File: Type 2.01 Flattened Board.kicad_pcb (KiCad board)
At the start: 4 copper layers, 170 x 170 mm, 70 parts, among them J1 Conn_02x28_Odd_Even, J2 Conn_01x02, J3 Conn_01x04, J4 Conn_02x03_Odd_Even, J5 Conn_02x03_Odd_Even, J6 Conn_02x28_Odd_Even, U1 74AHC74, U10 74AHC174, U11 74AHC245, U13 74AHC04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

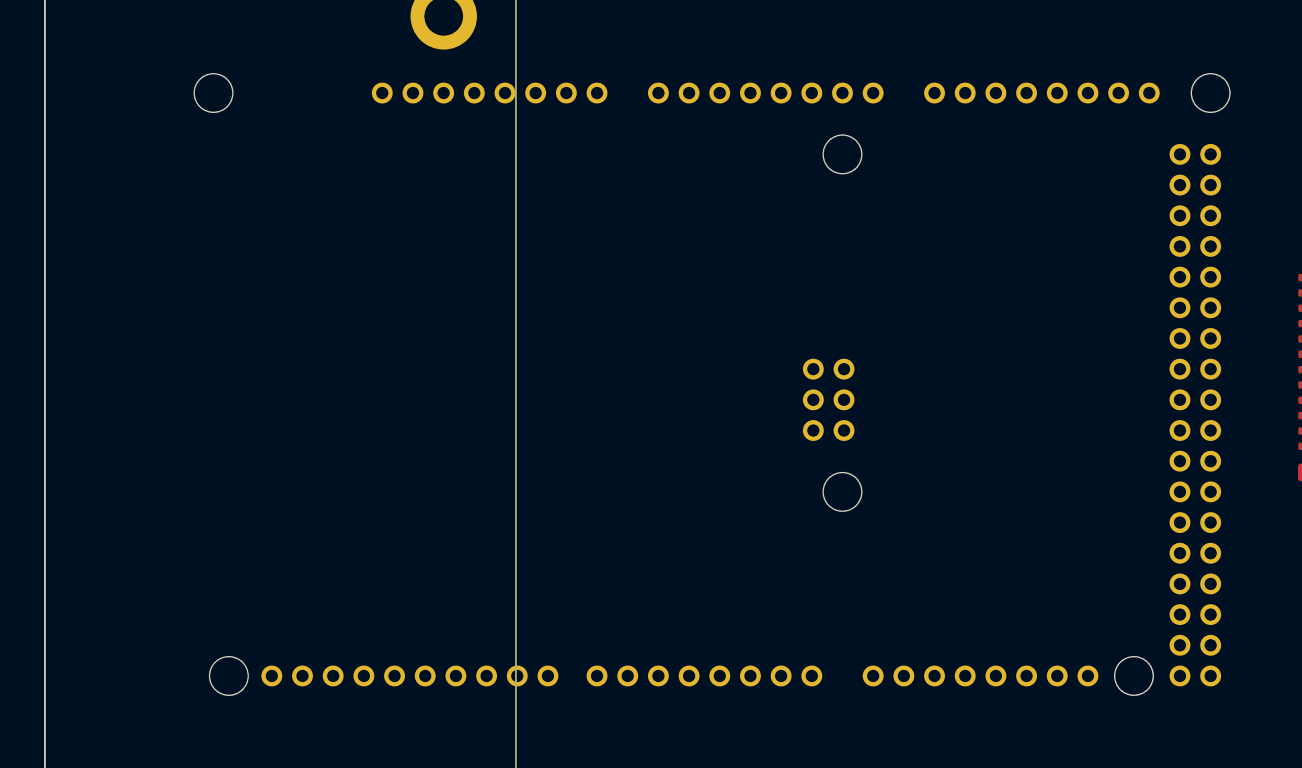
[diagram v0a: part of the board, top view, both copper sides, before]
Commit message: RTC socket removed, will be handled by the uno breakout area
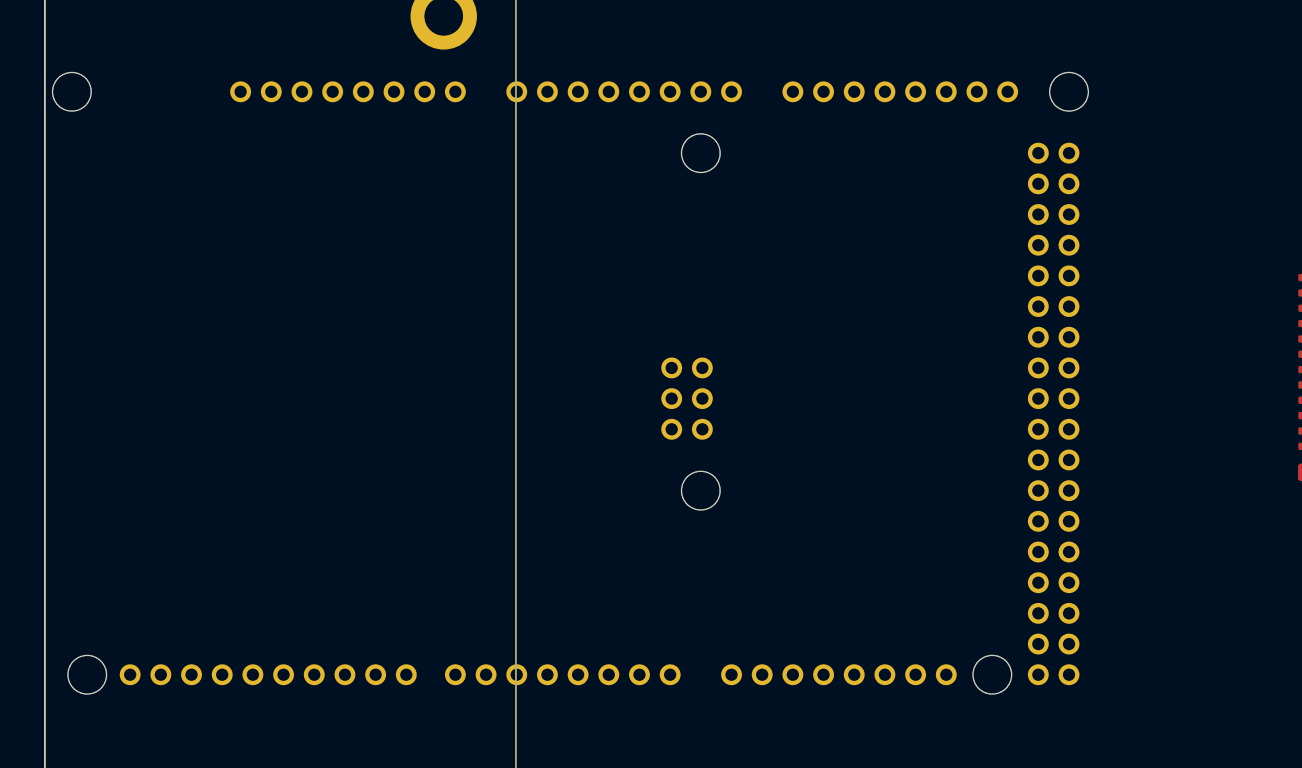
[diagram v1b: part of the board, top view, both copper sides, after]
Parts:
- moved XA1 11.7 mm to (-11.7, 10.1)
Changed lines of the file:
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@@
   )
   (footprint "Arduino_Alarm_Siren:Arduino_Mega2560_Shield" (layer "B.Cu")
-    (at -0.00762 10.157956)
+    (at -11.73484 10.05586)
     (descr "https://store.arduino.cc/arduino-mega-2560-rev3")
     (property "Sheetfile" "Type 2.01 Flattened Board.kicad_sch")

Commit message: Drop the HC125 and start redoing the pinout for the management engine to maximize layout capabilities
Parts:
- C4, U10: moved to B.Cu
- moved U14 192.9 mm to (247.3, 158.6), turned to 180 degrees
- moved C26 183.0 mm to (249.9, 147.2), turned to 90 degrees
- moved C27 153.5 mm to (249.9, 116.7), turned to 90 degrees
- moved C25 153.3 mm to (229.3, 137.0), turned to -90 degrees
- moved C30 77.0 mm to (140.9, 123.4)
- moved C31 77.0 mm to (130.7, 144.1)
- moved C32 77.0 mm to (161.2, 144.2)
- moved U16 77.0 mm to (119.3, 141.3)
- moved C1 51.5 mm to (79.0, 88.2), turned to 180 degrees
- moved C20 47.0 mm to (158.3, 131.5), turned to -90 degrees
- moved U1 41.8 mm to (71.8, 91.0), turned to 0 degrees
- moved U13 39.5 mm to (152.5, 133.4), turned to 90 degrees
- moved U10 20.9 mm to (91.5, 95.7), turned to 0 degrees
- moved U7 18.8 mm to (67.4, 72.7)
- moved C7 18.8 mm to (58.1, 76.8)
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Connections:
- U16 pad 1: /i960.~{BE0} -> unconnected-(U16-Pad1)
- U16 pad 16: /i960/ME.PD7 -> /i960.CLK
- U16 pad 2: /i960.~{BE1} -> unconnected-(U16-Pad2)
- U16 pad 3: /i960/i960.~{BLAST} -> unconnected-(U16-Pad3)
- U16 pad 33: /i960/ME.PA0 -> /i960.~{BE0}
- U16 pad 34: /i960/ME.PA1 -> /i960.~{BE1}
- U16 pad 35: /i960.CLK -> /i960/i960.~{BLAST}
- U16 pad 36: /i960/ME.PA3 -> /i960/FAIL_SIG
- U16 pad 4: /i960/FAIL_SIG -> unconnected-(U16-Pad4)

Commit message: Fix grouping
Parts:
- moved C20 49.3 mm to (128.1, 92.6), turned to 0 degrees
- moved U13 41.7 mm to (130.0, 98.3), turned to 180 degrees
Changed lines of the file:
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@@
   )
   (footprint "Package_SO:SOIC-14_3.9x8.7mm_P1.27mm" (layer "B.Cu")
-    (at 152.54478 133.36778 90)
+    (at 129.96672 98.30308 180)
     (descr "SOIC, 14 Pin (JEDEC MS-012AB, https://www.analog.com/media/en/package-pcb-resources/package/pkg_pdf/soic_narrow-r/r_14.pdf), generated with kicad-footprint-generator ipc_gullwing_generator.py")
     (tags "SOIC SO")
@@
     (property "Sheetname" "i960")
     (attr smd)
-    (fp_text reference "U13" (at -2.20218 5.3086 90) (layer "B.SilkS")
-      (effects (font (size 1 1) (thickness 0.15)) (justify mirror))
-    )
-    (fp_text value "74AHC04" (at 0 -5.28 90) (layer "B.Fab")
-      (effects (font (size 1 1) (thickness 0.15)) (justify mirror))
-    )
-    (fp_text user "${REFERENCE}" (at 0 0 90) (layer "B.Fab")
+    (fp_text reference "U13" (at -2.20218 5.3086) (layer "B.SilkS")
+      (effects (font (size 1 1) (thickness 0.15)) (justify mirror))
+    )
+    (fp_text value "74AHC04" (at 0 -5.28) (layer "B.Fab")
+      (effects (font (size 1 1) (thickness 0.15)) (justify mirror))
+    )
+    (fp_text user "${REFERENCE}" (at 0 0) (layer "B.Fab")
       (effects (font (size 0.98 0.98) (thickness 0.15)) (justify mirror))
     )
@@
     (fp_line (start -1.95 3.35) (end -0.975 4.325) (layer "B.Fab") (width 0.1))
     (fp_line (start -1.95 -4.325) (end -1.95 3.35) (layer "B.Fab") (width 0.1))
-    (pad "1" smd roundrect (at -2.475 3.81 90) (size 1.95 0.6) (layers "B.Cu" "B.Paste" "B.Mask") (roundrect_rratio 0.25))
-    (pad "2" smd roundrect (at -2.475 2.54 90) (size 1.95 0.6) (layers "B.Cu" "B.Paste" "B.Mask") (roundrect_rratio 0.25))
-    (pad "3" smd roundrect (at -2.475 1.27 90) (size 1.95 0.6) (layers "B.Cu" "B.Paste" "B.Mask") (roundrect_rratio 0.25)
+    (pad "1" smd roundrect (at -2.475 3.81 180) (size 1.95 0.6) (layers "B.Cu" "B.Paste" "B.Mask") (roundrect_rratio 0.25))
+    (pad "2" smd roundrect (at -2.475 2.54 180) (size 1.95 0.6) (layers "B.Cu" "B.Paste" "B.Mask") (roundrect_rratio 0.25))
+    (pad "3" smd roundrect (at -2.475 1.27 180) (size 1.95 0.6) (layers "B.Cu" "B.Paste" "B.Mask") (roundrect_rratio 0.25)
       (net 10 "/i960/~{RESET_INTERMEDIATE}") (pintype "input"))
-    (pad "4" smd roundrect (at -2.475 0 90) (size 1.95 0.6) (layers "B.Cu" "B.Paste" "B.Mask") (roundrect_rratio 0.25)
+    (pad "4" smd roundrect (at -2.475 0 180) (size 1.95 0.6) (layers "B.Cu" "B.Paste" "B.Mask") (roundrect_rratio 0.25)
       (net 51 "/i960/~{RESET960}") (pintype "output"))
-    (pad "5" smd roundrect (at -2.475 -1.27 90) (size 1.95 0.6) (layers "B.Cu" "B.Paste" "B.Mask") (roundrect_rratio 0.25)
+    (pad "5" smd roundrect (at -2.475 -1.27 180) (size 1.95 0.6) (layers "B.Cu" "B.Paste" "B.Mask") (roundrect_rratio 0.25)
       (net 63 "Net-(U13-Pad5)") (pintype "input"))
-    (pad "6" smd roundrect (at -2.475 -2.54 90) (size 1.95 0.6) (layers "B.Cu" "B.Paste" "B.Mask") (roundrect_rratio 0.25)
+    (pad "6" smd roundrect (at -2.475 -2.54 180) (size 1.95 0.6) (layers "B.Cu" "B.Paste" "B.Mask") (roundrect_rratio 0.25)
       (net 13 "/i960/i960.~{INT0}") (pintype "output"))
-    (pad "7" smd roundrect (at -2.475 -3.81 90) (size 1.95 0.6) (layers "B.Cu" "B.Paste" "B.Mask") (roundrect_rratio 0.25)
+    (pad "7" smd roundrect (at -2.475 -3.81 180) (size 1.95 0.6) (layers "B.Cu" "B.Paste" "B.Mask") (roundrect_rratio 0.25)
       (net 16 "GND") (pinfunction "GND") (pintype "power_in"))
-    (pad "8" smd roundrect (at 2.475 -3.81 90) (size 1.95 0.6) (layers "B.Cu" "B.Paste" "B.Mask") (roundrect_rratio 0.25)
+    (pad "8" smd roundrect (at 2.475 -3.81 180) (size 1.95 0.6) (layers "B.Cu" "B.Paste" "B.Mask") (roundrect_rratio 0.25)
       (net 14 "/i960/i960.~{INT3}") (pintype "output"))
-    (pad "9" smd roundrect (at 2.475 -2.54 90) (size 1.95 0.6) (layers "B.Cu" "B.Paste" "B.Mask") (roundrect_rratio 0.25)
+    (pad "9" smd roundrect (at 2.475 -2.54 180) (size 1.95 0.6) (layers "B.Cu" "B.Paste" "B.Mask") (roundrect_rratio 0.25)
       (net 64 "Net-(U13-Pad9)") (pintype "input"))
-    (pad "10" smd roundrect (at 2.475 -1.27 90) (size 1.95 0.6) (layers "B.Cu" "B.Paste" "B.Mask") (roundrect_rratio 0.25))
-    (pad "11" smd roundrect (at 2.475 0 90) (size 1.95 0.6) (layers "B.Cu" "B.Paste" "B.Mask") (roundrect_rratio 0.25))
-    (pad "12" smd roundrect (at 2.475 1.27 90) (size 1.95 0.6) (layers "B.Cu" "B.Paste" "B.Mask") (roundrect_rratio 0.25))
-    (pad "13" smd roundrect (at 2.475 2.54 90) (size 1.95 0.6) (layers "B.Cu" "B.Paste" "B.Mask") (roundrect_rratio 0.25))
-    (pad "14" smd roundrect (at 2.475 3.81 90) (size 1.95 0.6) (layers "B.Cu" "B.Paste" "B.Mask") (roundrect_rratio 0.25)
+    (pad "10" smd roundrect (at 2.475 -1.27 180) (size 1.95 0.6) (layers "B.Cu" "B.Paste" "B.Mask") (roundrect_rratio 0.25))
+    (pad "11" smd roundrect (at 2.475 0 180) (size 1.95 0.6) (layers "B.Cu" "B.Paste" "B.Mask") (roundrect_rratio 0.25))
+    (pad "12" smd roundrect (at 2.475 1.27 180) (size 1.95 0.6) (layers "B.Cu" "B.Paste" "B.Mask") (roundrect_rratio 0.25))
+    (pad "13" smd roundrect (at 2.475 2.54 180) (size 1.95 0.6) (layers "B.Cu" "B.Paste" "B.Mask") (roundrect_rratio 0.25))
+    (pad "14" smd roundrect (at 2.475 3.81 180) (size 1.95 0.6) (layers "B.Cu" "B.Paste" "B.Mask") (roundrect_rratio 0.25)
       (net 2 "+5V") (pinfunction "VCC") (pintype "power_in"))
     (model "${KICAD6_3DMODEL_DIR}/Package_SO.3dshapes/SOIC-14_3.9x8.7mm_P1.27mm.wrl"
@@
   )
   (footprint "Capacitor_SMD:C_0805_2012Metric_Pad1.18x1.45mm_HandSolder" (layer "B.Cu")
-    (at 158.28772 131.54914 -90)
+    (at 128.14808 92.56014)
     (descr "Capacitor SMD 0805 (2012 Metric), square (rectangular) end terminal, IPC_7351 nominal with elongated pad for handsoldering. (Body size source: IPC-SM-782 page 76, https://www.pcb-3d.com/wordpress/wp-content/uploads/ipc-sm-782a_amendment_1_and_2.pdf, https://docs.google.com/spreadsheets/d/1BsfQQcO9C6DZCsRaXUlFlo91Tg2WpOkGARC1WS5S8t0/edit?usp=sharing), generated with kicad-footprint-generator")
     (tags "capacitor handsolder")
@@
     (property "Sheetname" "i960")
     (attr smd)
-    (fp_text reference "C20" (at 0.00762 -1.98374 90) (layer "B.SilkS")
-      (effects (font (size 1 1) (thickness 0.15)) (justify mirror))
-    )
-    (fp_text value "0.1uF" (at 0 -1.68 90) (layer "B.Fab")
-      (effects (font (size 1 1) (thickness 0.15)) (justify mirror))
-    )
-    (fp_text user "${REFERENCE}" (at 0 0 90) (layer "B.Fab")
+    (fp_text reference "C20" (at 0.00762 -1.98374) (layer "B.SilkS")
+      (effects (font (size 1 1) (thickness 0.15)) (justify mirror))
+    )
+    (fp_text value "0.1uF" (at 0 -1.68) (layer "B.Fab")
+      (effects (font (size 1 1) (thickness 0.15)) (justify mirror))
+    )
+    (fp_text user "${REFERENCE}" (at 0 0) (layer "B.Fab")
       (effects (font (size 0.5 0.5) (thickness 0.08)) (justify mirror))
     )
@@
     (fp_line (start 1 -0.625) (end -1 -0.625) (layer "B.Fab") (width 0.1))
     (fp_line (start -1 -0.625) (end -1 0.625) (layer "B.Fab") (width 0.1))
-    (pad "1" smd roundrect (at -1.0375 0 270) (size 1.175 1.45) (layers "B.Cu" "B.Paste" "B.Mask") (roundrect_rratio 0.212766)
+    (pad "1" smd roundrect (at -1.0375 0) (size 1.175 1.45) (layers "B.Cu" "B.Paste" "B.Mask") (roundrect_rratio 0.212766)
       (net 2 "+5V") (pintype "passive"))
-    (pad "2" smd roundrect (at 1.0375 0 270) (size 1.175 1.45) (layers "B.Cu" "B.Paste" "B.Mask") (roundrect_rratio 0.212766)
+    (pad "2" smd roundrect (at 1.0375 0) (size 1.175 1.45) (layers "B.Cu" "B.Paste" "B.Mask") (roundrect_rratio 0.212766)
       (net 16 "GND") (pintype "passive"))
     (model "${KICAD6_3DMODEL_DIR}/Capacitor_SMD.3dshapes/C_0805_2012Metric.wrl"
@@
     )
   )
+  (group "" (id 66bbbecf-4bef-4f8f-9f0a-41f19fee23df)
+    (members
+      2807219c-2299-4b9a-820d-55024e19024e
+      3b9bf3ec-4bf9-464a-88b7-e696eb3390a8
+    )
+  )

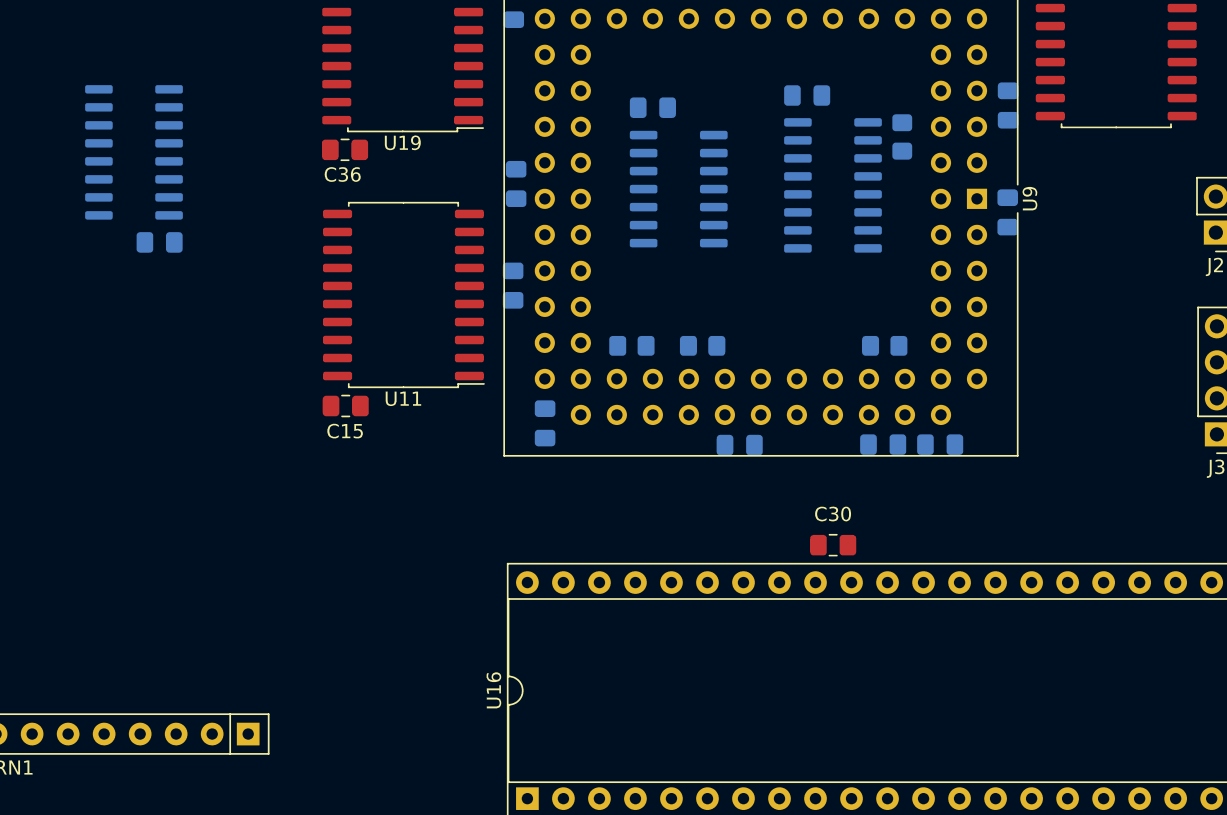
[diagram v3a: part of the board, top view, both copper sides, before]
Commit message: Drop the 74AHC174 because the edge detector is fine.
Also don't use a CCL for the reset detection. Instead, the two CCLs are
way more useful for generating the 10mhz signal cleanly.

I also am going do the reset circuit manually because it makes way more
sense that way. I am even going to use the builtin pullups as well!

I can also get rid of the ME_BOOTED pin. Still need to do that
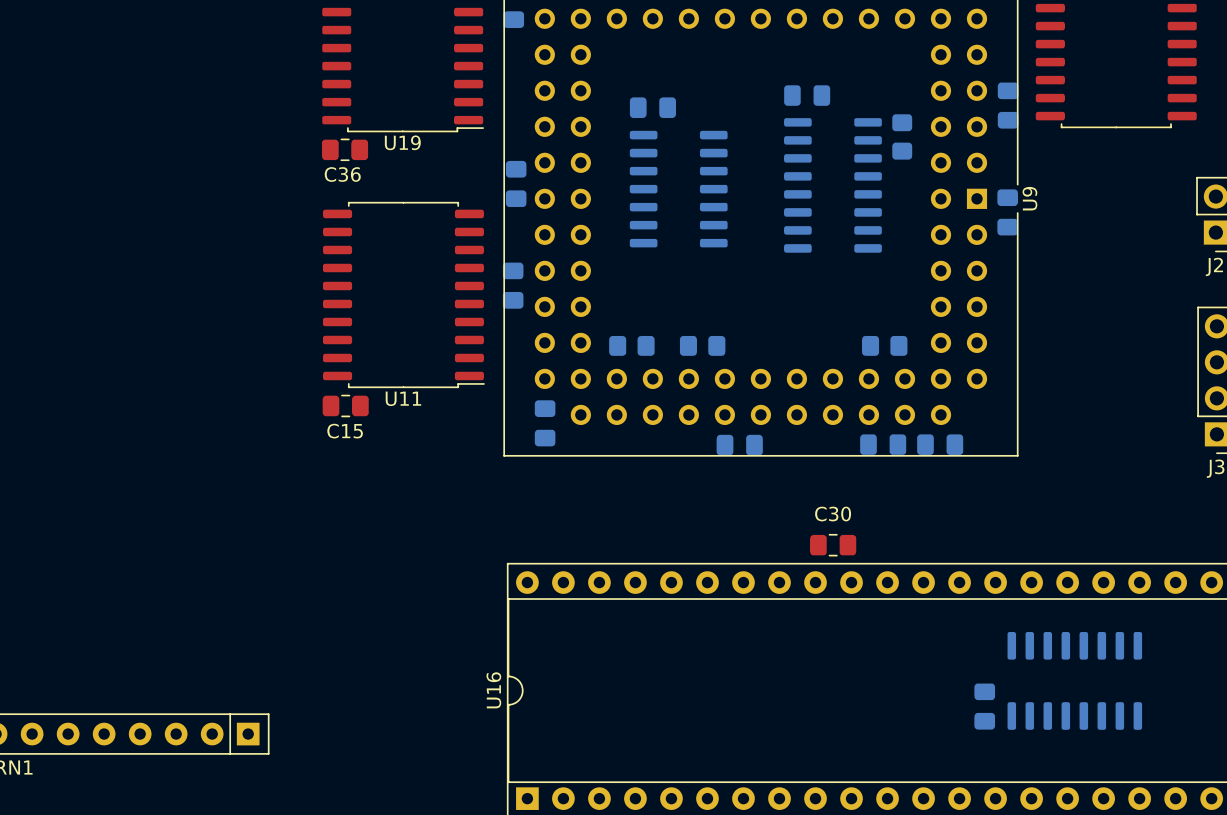
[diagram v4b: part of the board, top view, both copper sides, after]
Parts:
- moved U10 76.1 mm to (157.9, 133.0), turned to -90 degrees
- moved C4 66.8 mm to (151.6, 134.8), turned to 90 degrees
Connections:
- U16 pad 1: unconnected-(U16-Pad1) -> /i960/~{ME_BOOTED}
- U16 pad 10: /i960/EDGE_A -> /i960/ME.PD1
- U16 pad 11: /i960/~{ME_READY} -> /i960/ME.PD2
- U16 pad 12: /i960/~{READY960} -> /i960/ME.PD3
- U16 pad 2: unconnected-(U16-Pad2) -> /i960/~{PIC_BOOTED}
- U16 pad 23: /i960/~{ME_BOOTED} -> /i960/EDGE_B
- U16 pad 24: /i960/~{PIC_BOOTED} -> /i960/EDGE_A
- U16 pad 25: /i960/5V_~{CHIPSET_BOOTED} -> /i960/~{ME_READY}
- U16 pad 26: /i960/~{RESET_INTERMEDIATE} -> /i960/~{READY960}
- U16 pad 3: unconnected-(U16-Pad3) -> /i960/5V_~{CHIPSET_BOOTED}
- U16 pad 4: unconnected-(U16-Pad4) -> /i960/~{RESET_INTERMEDIATE}
- U16 pad 9: /i960/EDGE_B -> /i960/ME.PD0

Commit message: Increased simplicity
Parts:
- removed C4: 0.1uF, Capacitor_SMD:C_0805_2012Metric_Pad1.18x1.45mm_HandSolder
- removed U10: 74AHC174, Package_SO:SOIC-16_3.9x9.9mm_P1.27mm
- moved C30 6.98 mm to (134.1, 121.7)
- moved C31 6.98 mm to (123.9, 142.4)
- moved C32 6.98 mm to (154.5, 142.4)
- moved U16 6.98 mm to (112.5, 139.6)
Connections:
- RN1 pad 10: /i960/PU2 -> unconnected-(RN1-Pad10)
- RN1 pad 11: /i960/PU3 -> unconnected-(RN1-Pad11)
- RN1 pad 12: /i960/~{MR_{0}} -> unconnected-(RN1-Pad12)
- RN1 pad 2: /i960/~{ME_BOOTED} -> /i960/~{RESET_INTERMEDIATE}
- RN1 pad 3: /i960/~{PIC_BOOTED} -> /i960/5V_~{RESET}
- RN1 pad 4: /i960/~{RESET_INTERMEDIATE} -> /i960/~{CLK_READY}
- RN1 pad 5: /i960/5V_~{CHIPSET_BOOTED} -> /i960/PU0
- RN1 pad 6: /i960/5V_~{RESET} -> /i960/PU1
- RN1 pad 7: /i960/~{CLK_READY} -> /i960/PU2
- RN1 pad 8: /i960/PU0 -> /i960/PU3
- RN1 pad 9: /i960/PU1 -> unconnected-(RN1-Pad9)
- U1 pad 1: /i960/PU1 -> (no net)
- U1 pad 2: Net-(U1-Pad2) -> (no net)
- U1 pad 3: /i960.CLK2 -> (no net)
- U1 pad 4: /i960/PU0 -> (no net)
- U1 pad 5: /i960.CLK -> (no net)
- U1 pad 6: Net-(U1-Pad2) -> (no net)
- U13 pad 1: (no net) -> Net-(U13-Pad1)
- U13 pad 2: (no net) -> /i960/~{READY960}
- U16 pad 1: /i960/~{ME_BOOTED} -> /i960/~{PIC_BOOTED}
- U16 pad 10: /i960/ME.PD1 -> /i960.~{BE1}
- U16 pad 11: /i960/ME.PD2 -> /i960/i960.~{BLAST}
- U16 pad 12: /i960/ME.PD3 -> /i960/FAIL_SIG
- U16 pad 16: /i960.CLK -> /i960/ME.PD7
- U16 pad 2: /i960/~{PIC_BOOTED} -> /i960/5V_~{CHIPSET_BOOTED}
- U16 pad 23: /i960/EDGE_B -> /i960/~{ME_READY}
- U16 pad 24: /i960/EDGE_A -> /i960/ME.PF1
- U16 pad 25: /i960/~{ME_READY} -> /i960/ME.PF2
- U16 pad 26: /i960/~{READY960} -> Net-(U13-Pad1)
- U16 pad 3: /i960/5V_~{CHIPSET_BOOTED} -> /i960/ME.PC2
- U16 pad 33: /i960.~{BE0} -> /i960/ME.PA0
- U16 pad 34: /i960.~{BE1} -> /i960/ME.PA1
- U16 pad 35: /i960/i960.~{BLAST} -> /i960/ME.PA2
- U16 pad 36: /i960/FAIL_SIG -> /i960.CLK
- U16 pad 9: /i960/ME.PD0 -> /i960.~{BE0}

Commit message: Place components around the cpu as much as possible
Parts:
- moved U14 186.8 mm to (141.3, 4.76), turned to 0 degrees
- moved C26 172.0 mm to (138.7, 16.1), turned to -90 degrees
- moved RN1 136.3 mm to (132.1, 4.39), turned to -90 degrees
- moved C27 131.4 mm to (138.7, 46.7), turned to -90 degrees
- moved C25 131.0 mm to (159.3, 26.3), turned to 90 degrees
- moved J4 123.8 mm to (102.8, 14.5), turned to 90 degrees
- moved C1 72.4 mm to (108.6, 22.1)
- moved U1 72.4 mm to (101.4, 25.0)
- moved C20 61.6 mm to (83.8, 135.4), turned to 90 degrees
- moved R4 60.9 mm to (95.0, 128.3), turned to 0 degrees
- moved C24 55.8 mm to (106.6, 130.7)
- moved C29 55.8 mm to (87.7, 147.1)
- moved U18 55.8 mm to (81.9, 104.9)
- moved U9 55.8 mm to (104.4, 129.8)
- moved C12 55.8 mm to (95.5, 112.4)
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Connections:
- U13 pad 1: Net-(U13-Pad1) -> Net-(U17-Pad4)
- U13 pad 12: (no net) -> /i960/~{RESET960}
- U13 pad 13: (no net) -> /i960/~{RESET_INTERMEDIATE}
- U13 pad 2: /i960/~{READY960} -> /i960/i960.~{INT0}
- U13 pad 3: /i960/~{RESET_INTERMEDIATE} -> Net-(U17-Pad12)
- U13 pad 4: /i960/~{RESET960} -> /i960/i960.~{INT3}
- U13 pad 5: Net-(U13-Pad5) -> (no net)
- U13 pad 6: /i960/i960.~{INT0} -> (no net)
- U13 pad 8: /i960/i960.~{INT3} -> /i960/~{READY960}
- U13 pad 9: Net-(U13-Pad9) -> Net-(U16-Pad26)
- U16 pad 26: Net-(U13-Pad1) -> Net-(U16-Pad26)
- U17 pad 12: Net-(U13-Pad9) -> Net-(U17-Pad12)
- U17 pad 4: Net-(U13-Pad5) -> Net-(U17-Pad4)
